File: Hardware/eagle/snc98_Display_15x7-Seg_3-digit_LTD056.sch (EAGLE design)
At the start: 76 parts, among them M10 IRLML2244, M11 IRLML2244, M4 IRLML2244, M5 IRLML2244, M6 IRLML2244, M7 IRLML2244, M8 IRLML2244, M9 IRLML2244, X1 MICROMATCH-12, X2 MICROMATCH-14, X3 MICROMATCH-12, X4 MICROMATCH-14

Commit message: V 5.0 Hardware - Design
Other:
- note added: "V 5.0"
- note removed: "1.0"
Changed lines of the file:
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@@
 <grid distance="0.1" unitdist="inch" unit="inch" style="lines" multiple="1" display="yes" altdistance="0.05" altunitdist="inch" altunit="inch"/>
 <layers>
-<layer number="1" name="Top" color="4" fill="1" visible="yes" active="no"/>
-<layer number="2" name="Route2" color="1" fill="3" visible="yes" active="no"/>
-<layer number="3" name="Route3" color="4" fill="3" visible="yes" active="no"/>
-<layer number="4" name="Route4" color="1" fill="4" visible="yes" active="no"/>
-<layer number="5" name="Route5" color="4" fill="4" visible="yes" active="no"/>
-<layer number="6" name="Route6" color="1" fill="8" visible="yes" active="no"/>
-<layer number="7" name="Route7" color="4" fill="8" visible="yes" active="no"/>
-<layer number="8" name="Route8" color="1" fill="2" visible="yes" active="no"/>
-<layer number="9" name="Route9" color="4" fill="2" visible="yes" active="no"/>
-<layer number="10" name="Route10" color="1" fill="7" visible="yes" active="no"/>
-<layer number="11" name="Route11" color="4" fill="7" visible="yes" active="no"/>
-<layer number="12" name="Route12" color="1" fill="5" visible="yes" active="no"/>
-<layer number="13" name="Route13" color="4" fill="5" visible="yes" active="no"/>
-<layer number="14" name="Route14" color="1" fill="6" visible="yes" active="no"/>
-<layer number="15" name="Route15" color="4" fill="6" visible="yes" active="no"/>
-<layer number="16" name="Bottom" color="1" fill="1" visible="yes" active="no"/>
-<layer number="17" name="Pads" color="2" fill="1" visible="yes" active="no"/>
-<layer number="18" name="Vias" color="2" fill="1" visible="yes" active="no"/>
-<layer number="19" name="Unrouted" color="6" fill="1" visible="yes" active="no"/>
-<layer number="20" name="Dimension" color="15" fill="1" visible="yes" active="no"/>
-<layer number="21" name="tPlace" color="16" fill="1" visible="yes" active="no"/>
-<layer number="22" name="bPlace" color="14" fill="1" visible="yes" active="no"/>
-<layer number="23" name="tOrigins" color="15" fill="1" visible="yes" active="no"/>
-<layer number="24" name="bOrigins" color="15" fill="1" visible="yes" active="no"/>
-<layer number="25" name="tNames" color="7" fill="1" visible="yes" active="no"/>
-<layer number="26" name="bNames" color="7" fill="1" visible="yes" active="no"/>
-<layer number="27" name="tValues" color="7" fill="1" visible="yes" active="no"/>
-<layer number="28" name="bValues" color="7" fill="1" visible="yes" active="no"/>
+<layer number="1" name="Top" color="4" fill="1" visible="no" active="no"/>
+<layer number="2" name="Route2" color="1" fill="3" visible="no" active="no"/>
+<layer number="3" name="Route3" color="4" fill="3" visible="no" active="no"/>
+<layer number="4" name="Route4" color="1" fill="4" visible="no" active="no"/>
+<layer number="5" name="Route5" color="4" fill="4" visible="no" active="no"/>
+<layer number="6" name="Route6" color="1" fill="8" visible="no" active="no"/>
+<layer number="7" name="Route7" color="4" fill="8" visible="no" active="no"/>
+<layer number="8" name="Route8" color="1" fill="2" visible="no" active="no"/>
+<layer number="9" name="Route9" color="4" fill="2" visible="no" active="no"/>
+<layer number="10" name="Route10" color="1" fill="7" visible="no" active="no"/>
+<layer number="11" name="Route11" color="4" fill="7" visible="no" active="no"/>
+<layer number="12" name="Route12" color="1" fill="5" visible="no" active="no"/>
+<layer number="13" name="Route13" color="4" fill="5" visible="no" active="no"/>
+<layer number="14" name="Route14" color="1" fill="6" visible="no" active="no"/>
+<layer number="15" name="Route15" color="4" fill="6" visible="no" active="no"/>
+<layer number="16" name="Bottom" color="1" fill="1" visible="no" active="no"/>
+<layer number="17" name="Pads" color="2" fill="1" visible="no" active="no"/>
+<layer number="18" name="Vias" color="2" fill="1" visible="no" active="no"/>
+<layer number="19" name="Unrouted" color="6" fill="1" visible="no" active="no"/>
+<layer number="20" name="Dimension" color="15" fill="1" visible="no" active="no"/>
+<layer number="21" name="tPlace" color="16" fill="1" visible="no" active="no"/>
+<layer number="22" name="bPlace" color="14" fill="1" visible="no" active="no"/>
+<layer number="23" name="tOrigins" color="15" fill="1" visible="no" active="no"/>
+<layer number="24" name="bOrigins" color="15" fill="1" visible="no" active="no"/>
+<layer number="25" name="tNames" color="7" fill="1" visible="no" active="no"/>
+<layer number="26" name="bNames" color="7" fill="1" visible="no" active="no"/>
+<layer number="27" name="tValues" color="7" fill="1" visible="no" active="no"/>
+<layer number="28" name="bValues" color="7" fill="1" visible="no" active="no"/>
 <layer number="29" name="tStop" color="7" fill="3" visible="no" active="no"/>
 <layer number="30" name="bStop" color="7" fill="6" visible="no" active="no"/>
@@
 <layer number="35" name="tGlue" color="7" fill="4" visible="no" active="no"/>
 <layer number="36" name="bGlue" color="7" fill="5" visible="no" active="no"/>
-<layer number="37" name="tTest" color="7" fill="1" visible="yes" active="no"/>
-<layer number="38" name="bTest" color="7" fill="1" visible="yes" active="no"/>
+<layer number="37" name="tTest" color="7" fill="1" visible="no" active="no"/>
+<layer number="38" name="bTest" color="7" fill="1" visible="no" active="no"/>
 <layer number="39" name="tKeepout" color="4" fill="11" visible="no" active="no"/>
 <layer number="40" name="bKeepout" color="1" fill="11" visible="no" active="no"/>
@@
 <layer number="44" name="Drills" color="7" fill="1" visible="no" active="no"/>
 <layer number="45" name="Holes" color="7" fill="1" visible="no" active="no"/>
-<layer number="46" name="Milling" color="3" fill="1" visible="yes" active="no"/>
-<layer number="47" name="Measures" color="7" fill="1" visible="yes" active="no"/>
-<layer number="48" name="Document" color="7" fill="1" visible="yes" active="no"/>
-<layer number="49" name="Reference" color="7" fill="1" visible="yes" active="no"/>
-<layer number="50" name="dxf" color="7" fill="1" visible="yes" active="no"/>
-<layer number="51" name="tDocu" color="6" fill="1" visible="yes" active="no"/>
-<layer number="52" name="bDocu" color="7" fill="1" visible="yes" active="no"/>
-<layer number="53" name="tGND_GNDA" color="7" fill="9" visible="yes" active="no"/>
-<layer number="54" name="bGND_GNDA" color="1" fill="9" visible="yes" active="no"/>
-<layer number="56" name="wert" color="7" fill="1" visible="yes" active="no"/>
-<layer number="57" name="tCAD" color="7" fill="1" visible="yes" active="no"/>
-<layer number="59" name="tCarbon" color="7" fill="1" visible="yes" active="no"/>
-<layer number="60" name="bCarbon" color="7" fill="1" visible="yes" active="no"/>
+<layer number="46" name="Milling" color="3" fill="1" visible="no" active="no"/>
+<layer number="47" name="Measures" color="7" fill="1" visible="no" active="no"/>
+<layer number="48" name="Document" color="7" fill="1" visible="no" active="no"/>
+<layer number="49" name="Reference" color="7" fill="1" visible="no" active="no"/>
+<layer number="50" name="dxf" color="7" fill="1" visible="no" active="no"/>
+<layer number="51" name="tDocu" color="6" fill="1" visible="no" active="no"/>
+<layer number="52" name="bDocu" color="7" fill="1" visible="no" active="no"/>
+<layer number="53" name="tGND_GNDA" color="7" fill="9" visible="no" active="no"/>
+<layer number="54" name="bGND_GNDA" color="1" fill="9" visible="no" active="no"/>
+<layer number="56" name="wert" color="7" fill="1" visible="no" active="no"/>
+<layer number="57" name="tCAD" color="7" fill="1" visible="no" active="no"/>
+<layer number="59" name="tCarbon" color="7" fill="1" visible="no" active="no"/>
+<layer number="60" name="bCarbon" color="7" fill="1" visible="no" active="no"/>
 <layer number="90" name="Modules" color="7" fill="1" visible="yes" active="yes"/>
 <layer number="91" name="Nets" color="2" fill="1" visible="yes" active="yes"/>
@@
 <text x="149.86" y="30.48" size="3.81" layer="91" ratio="12">Calculator 15-Digit with 1284P</text>
 <text x="149.86" y="25.4" size="2.54" layer="91" ratio="12">by Jens Grabner</text>
-<text x="238.76" y="7.62" size="2.54" layer="91" ratio="12">1.0</text>
+<text x="236.22" y="7.62" size="2.54" layer="91" ratio="12">V 5.0</text>
 <text x="5.08" y="10.16" size="2.1844" layer="91" ratio="10">Calculator 15-Digit with ATmega1284P by Jens Grabner is licensed under</text>
 <text x="5.08" y="15.24" size="3.81" layer="91" ratio="12">Copyright CERN 2013</text>
@@
 <text x="-58.42" y="58.42" size="3.81" layer="91" ratio="12">Calculator 15-Digit with 1284P</text>
 <text x="-58.42" y="53.34" size="2.54" layer="91" ratio="12">by Jens Grabner</text>
-<text x="30.48" y="35.56" size="2.54" layer="91" ratio="12">1.0</text>
+<text x="27.94" y="35.56" size="2.54" layer="91" ratio="12">V 5.0</text>
 <text x="-203.2" y="38.1" size="2.1844" layer="91" ratio="10">Calculator 15-Digit with ATmega1284P by Jens Grabner is licensed under</text>
 <text x="-203.2" y="43.18" size="3.81" layer="91" ratio="12">Copyright CERN 2013</text>

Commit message: sinh()_cosh()_tanh() added
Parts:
- BH4, BH5, BH6, JP1, JP10, JP11, JP12, JP2, JP7, JP8, JP9, LED1, LED2, LED3, LED4, LED5, LOGO1, LOGO3, R1, R10, R11, R12, R13, R14, R15, R16, R17, R18, R19, R2, R20, R21, R22, R23, R24, R25, R26, R27, R28, R29, R3, R30, R31, R32, R36, R37, R38, R39, R4, R40, R41, R42, R43, R5, R54, R55, R56, R57, R58, R59, R6, R7, R8, R9: OC_FARNELL (none) -> unknown
- M10, M11, M4, M5, M6, M7, M8, M9: MF (none) -> INFINEON; MPN (none) -> IRLML2244TRPBF; OC_FARNELL (none) -> 2468051
- X1, X2, X3, X4: MF (none) -> AMP - TE CONNECTIVITY

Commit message: Gerber file added
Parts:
- added R33, R34, R35, R44, R45, R46, R47, R48: 3k3, rcl:R-EU_M0805
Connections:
- net CA_LED: now also R33.1, R34.1, R35.1, R44.1, R45.1, R46.1, R47.1, R48.1
- net IO-A: now also R33.2
- net IO-B: now also R34.2
- net IO-C: now also R47.2
- net IO-D: now also R35.2
- net IO-DP: now also R46.2
- net IO-E: now also R48.2
- net IO-F: now also R44.2
- net IO-G: now also R45.2
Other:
- note added: "+ 2x DS1016-14MASIBB - Stecker;IDC;weiblich;PIN:14;IDC;für Flachkabel;1,27mm"
- moved on the sheet: M10, M11, M4, M5, M7, M9, R29, R30, R36, R37, R38, R39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

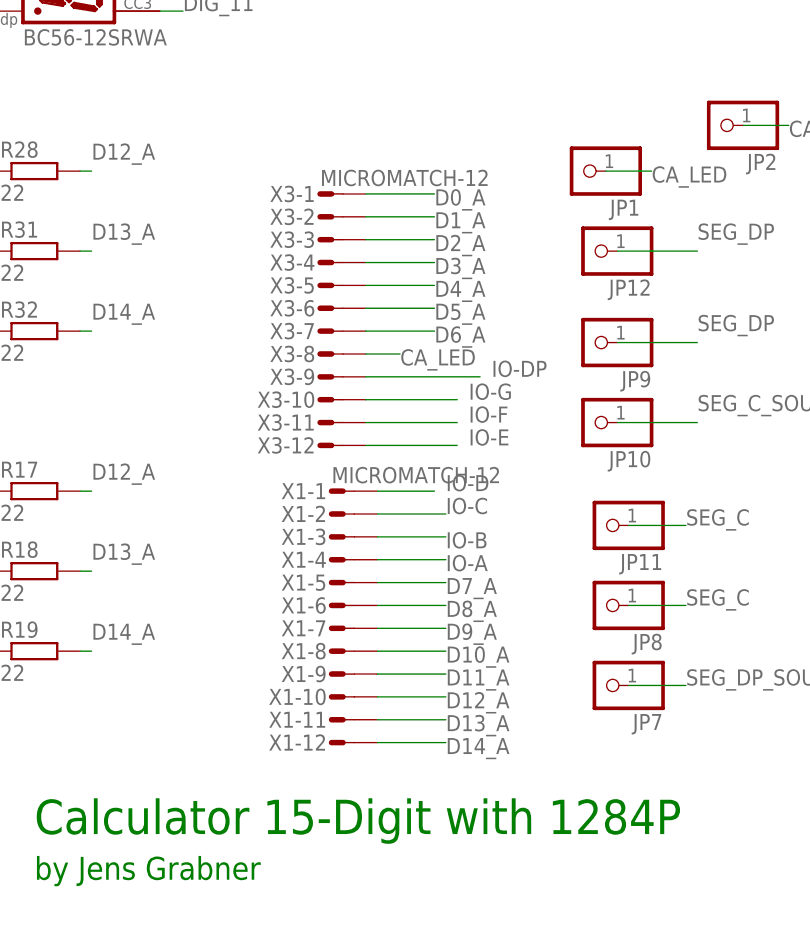
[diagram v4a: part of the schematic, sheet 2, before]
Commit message: more accurate Factorial Function n!
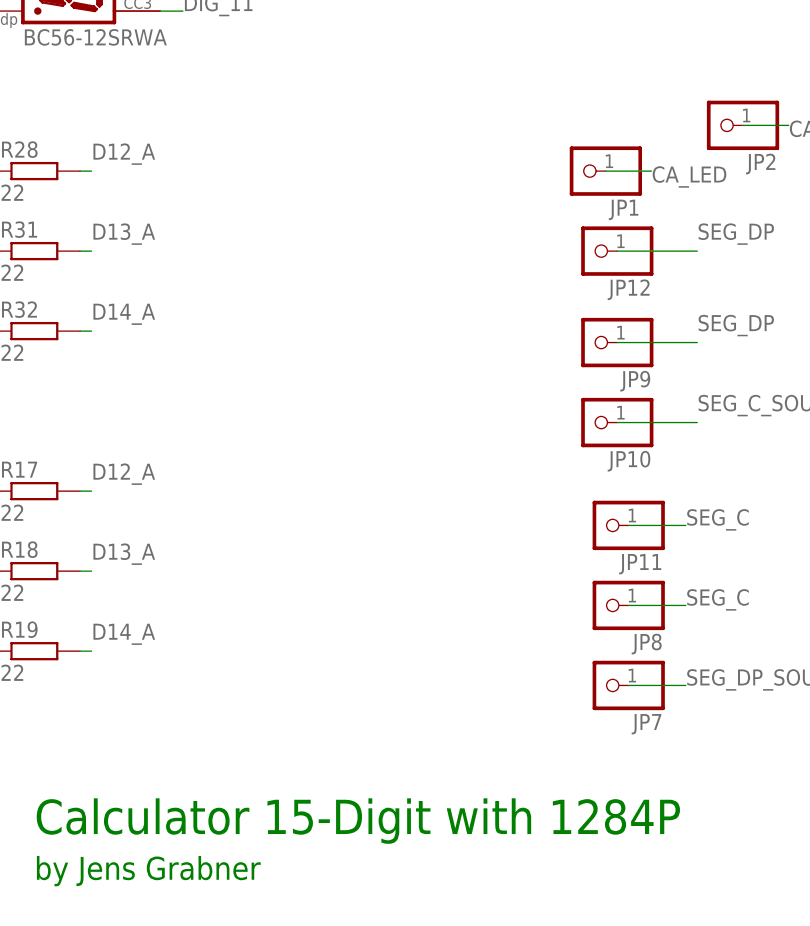
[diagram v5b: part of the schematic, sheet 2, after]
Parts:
- removed X1, X3: MICROMATCH-12, Con-amp-micromatch:MICROMATCH-12
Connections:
- net CA_LED: no longer X3-8.S
- net D0_A: no longer X3-1.S
- net D10_A: no longer X1-8.S
- net D11_A: no longer X1-9.S
- net D12_A: no longer X1-10.S
- net D13_A: no longer X1-11.S
- net D14_A: no longer X1-12.S
- net D1_A: no longer X3-2.S
- net D2_A: no longer X3-3.S
- net D3_A: no longer X3-4.S
- net D4_A: no longer X3-5.S
- net D5_A: no longer X3-6.S
- net D6_A: no longer X3-7.S
- net D7_A: no longer X1-5.S
- net D8_A: no longer X1-6.S
- net D9_A: no longer X1-7.S
- net IO-A: no longer X1-4.S
- net IO-B: no longer X1-3.S
- net IO-C: no longer X1-2.S
- net IO-D: no longer X1-1.S
- net IO-DP: no longer X3-9.S
- net IO-E: no longer X3-12.S
- net IO-F: no longer X3-11.S
- net IO-G: no longer X3-10.S

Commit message: cleanup_PCB
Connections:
- net SEG_C: no longer JP8.1
- net SEG_C_SOURCE: now also JP8.1
- net SEG_DP: now also JP7.1
- net SEG_DP_SOURCE: no longer JP7.1
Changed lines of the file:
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@@
 <setting verticaltext="up"/>
 </settings>
-<grid distance="0.1" unitdist="inch" unit="inch" style="lines" multiple="1" display="yes" altdistance="0.05" altunitdist="inch" altunit="inch"/>
+<grid distance="50" unitdist="mil" unit="mil" style="lines" multiple="1" display="yes" altdistance="0.05" altunitdist="inch" altunit="inch"/>
 <layers>
 <layer number="1" name="Top" color="4" fill="1" visible="no" active="no"/>
@@
 <segment>
 <pinref part="JP9" gate="G$1" pin="1"/>
-<wire x1="6.35" y1="113.03" x2="15.24" y2="113.03" width="0.1524" layer="91"/>
 <label x="15.24" y="114.3" size="1.778" layer="95"/>
-</segment>
-<segment>
-<pinref part="JP12" gate="G$1" pin="1"/>
-<wire x1="6.35" y1="123.19" x2="15.24" y2="123.19" width="0.1524" layer="91"/>
-<label x="15.24" y="124.46" size="1.778" layer="95"/>
+<wire x1="6.35" y1="113.03" x2="13.97" y2="113.03" width="0.1524" layer="91"/>
 </segment>
 <segment>
@@
 <pinref part="LED5" gate="DIG1" pin="DP"/>
 </segment>
+<segment>
+<pinref part="JP7" gate="G$1" pin="1"/>
+<label x="13.97" y="74.93" size="1.778" layer="95"/>
+<pinref part="JP12" gate="G$1" pin="1"/>
+<label x="15.24" y="124.46" size="1.778" layer="95"/>
+<wire x1="6.35" y1="123.19" x2="36.83" y2="123.19" width="0.1524" layer="91"/>
+<wire x1="36.83" y1="123.19" x2="36.83" y2="74.93" width="0.1524" layer="91"/>
+<wire x1="36.83" y1="74.93" x2="7.62" y2="74.93" width="0.1524" layer="91"/>
+</segment>
 </net>
 <net name="SEG_F" class="0">
@@
 <net name="SEG_C" class="0">
 <segment>
-<pinref part="JP8" gate="G$1" pin="1"/>
-<wire x1="7.62" y1="83.82" x2="13.97" y2="83.82" width="0.1524" layer="91"/>
-<label x="13.97" y="83.82" size="1.778" layer="95"/>
-</segment>
-<segment>
 <pinref part="JP11" gate="G$1" pin="1"/>
 <wire x1="7.62" y1="92.71" x2="13.97" y2="92.71" width="0.1524" layer="91"/>
@@
 </segment>
 </net>
-<net name="SEG_DP_SOURCE" class="0">
-<segment>
-<pinref part="JP7" gate="G$1" pin="1"/>
-<wire x1="7.62" y1="74.93" x2="13.97" y2="74.93" width="0.1524" layer="91"/>
-<label x="13.97" y="74.93" size="1.778" layer="95"/>
-</segment>
-</net>
 <net name="SEG_C_SOURCE" class="0">
 <segment>
 <pinref part="JP10" gate="G$1" pin="1"/>
-<wire x1="6.35" y1="104.14" x2="15.24" y2="104.14" width="0.1524" layer="91"/>
 <label x="15.24" y="105.41" size="1.778" layer="95"/>
-</segment>
-</net>
+<wire x1="6.35" y1="104.14" x2="34.29" y2="104.14" width="0.1524" layer="91"/>
+<wire x1="34.29" y1="104.14" x2="34.29" y2="83.82" width="0.1524" layer="91"/>
+<pinref part="JP8" gate="G$1" pin="1"/>
+<label x="13.97" y="83.82" size="1.778" layer="95"/>
+<wire x1="34.29" y1="83.82" x2="7.62" y2="83.82" width="0.1524" layer="91"/>
+</segment>
+</net>
